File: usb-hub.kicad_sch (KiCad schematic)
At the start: 15 parts, among them U302 CH334P, Y900 12Mhz

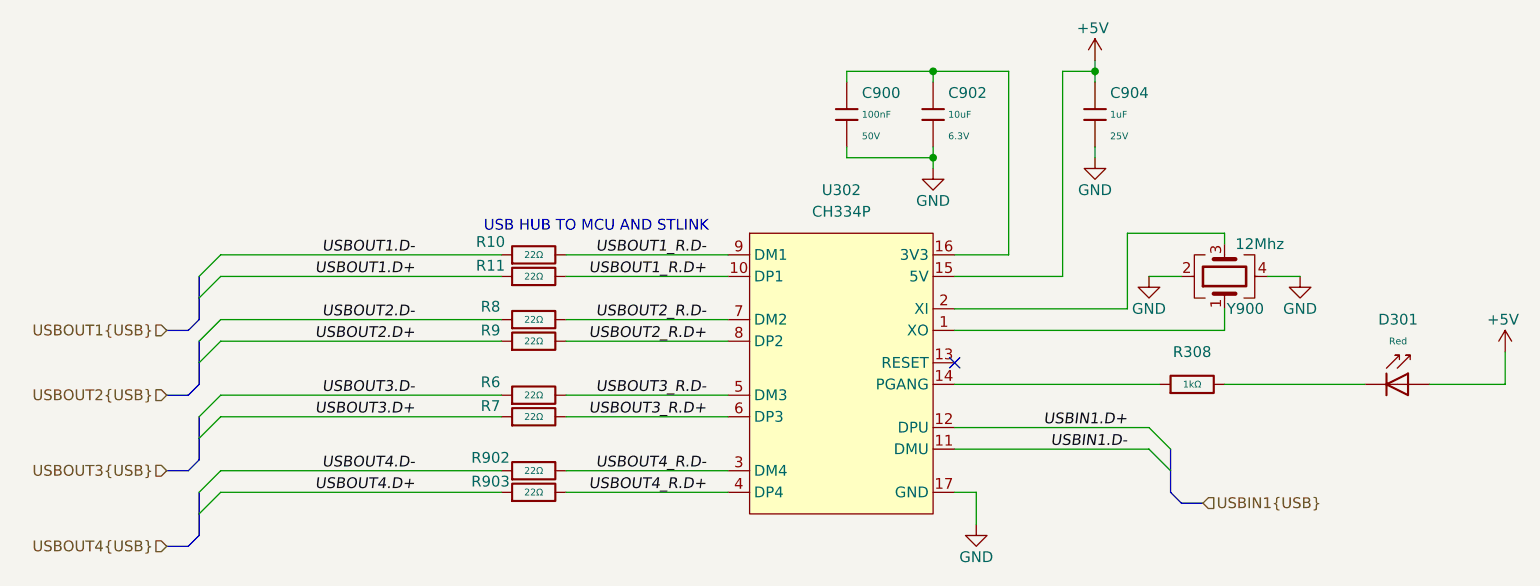
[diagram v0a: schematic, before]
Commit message: [#1] WIP: Change components to ones from the global library, refactor schematic
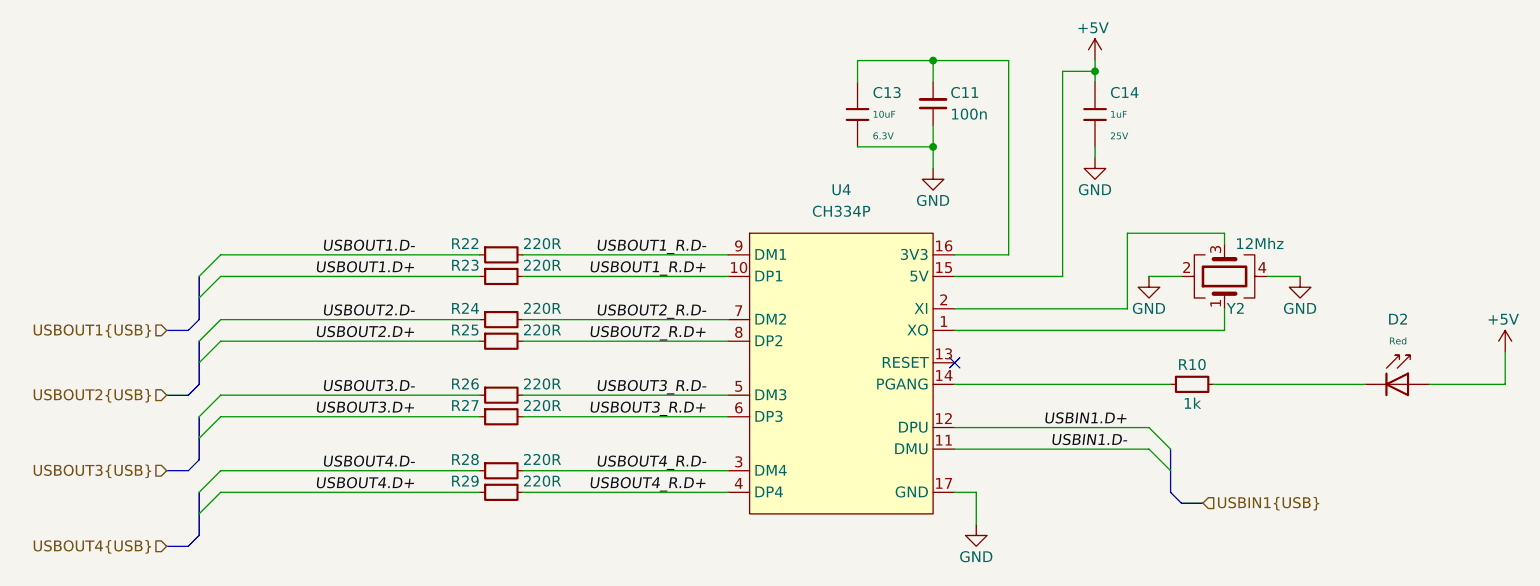
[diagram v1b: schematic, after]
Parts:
- removed C900: 100nF, PCM_JLCPCB:C_0402, symbol PCM_JLCPCB-Capacitors:0402,100nF,(2)
- removed R10, R11, R6, R7, R8, R9, R902, R903: 22Ω, PCM_JLCPCB:R_0402, symbol PCM_JLCPCB-Resistors:0402,22Ω
- removed R308: 1kΩ, PCM_JLCPCB:R_0402, symbol PCM_JLCPCB-Resistors:0402,1kΩ
- added C11: C-100n-0402, DW-footprints:C_0402_1005Metric, symbol DW-capacitors:C-100n-0402
- added R10: R-1k-0402, DW-footprints:R_0402_1005Metric, symbol DW-resistors:R-1k-0402
- added R22, R23, R24, R25, R26, R27, R28, R29: R-220r-0402, DW-footprints:R_0402_1005Metric, symbol DW-resistors:R-220r-0402
- renumbered C902 to C13, C904 to C14, D301 to D2, U302 to U4, Y900 to Y2
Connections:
- net GND: now also C11.1
- net USBOUT1.D+: now also R23.1
- net USBOUT1.D-: now also R22.1
- net USBOUT1_R.D+: now also R23.2
- net USBOUT1_R.D-: now also R22.2
- net USBOUT2.D+: now also R25.1
- net USBOUT2.D-: now also R24.1
- net USBOUT2_R.D+: now also R25.2
- net USBOUT2_R.D-: now also R24.2
- net USBOUT3.D+: now also R27.1
- net USBOUT3.D-: now also R26.1
- net USBOUT3_R.D+: now also R27.2
- net USBOUT3_R.D-: now also R26.2
- net USBOUT4.D+: now also R29.1
- net USBOUT4.D-: now also R28.1
- net USBOUT4_R.D+: now also R29.2
- net USBOUT4_R.D-: now also R28.2
- net at C13.1, U4.16 (3V3): now also C11.2
- net at U4.14 (PGANG): now also R10.1
- net at D2.1: now also R10.2
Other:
- note removed: "USB HUB TO MCU AND STLINK"
- moved on the sheet: C13
